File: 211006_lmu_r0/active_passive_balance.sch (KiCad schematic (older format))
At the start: 30 parts

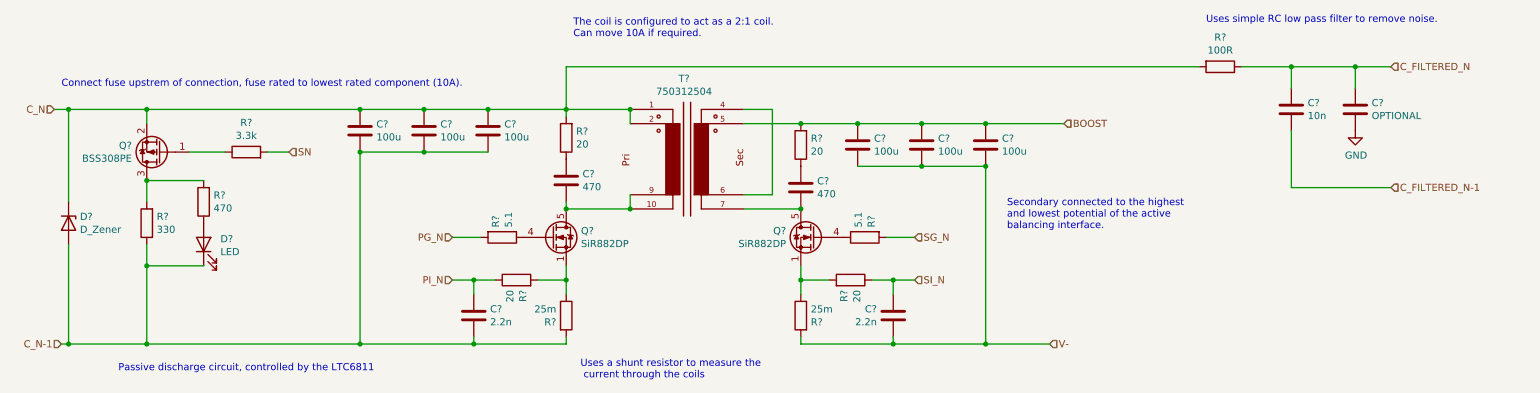
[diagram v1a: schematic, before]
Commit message: Updated BOM and footprints for non-hv components
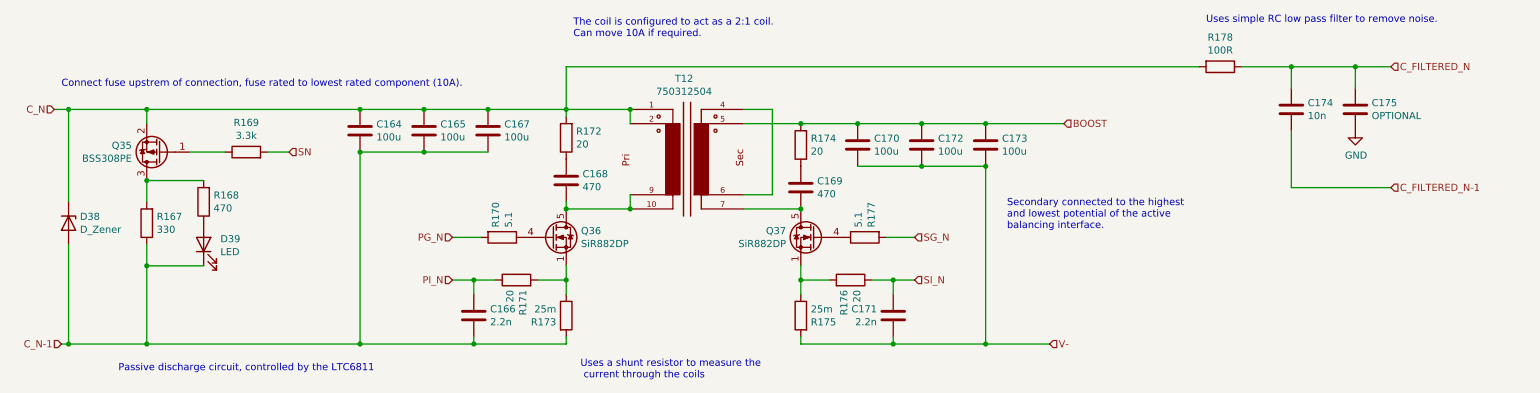
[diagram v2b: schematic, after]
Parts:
- gave numbers to parts that had none: 30

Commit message: Added most footprint requirements in HV
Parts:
- removed D19: D_Zener, symbol Device:D_Zener
- added D15: SBR10U200P5-13, DIO_SBR10U200P5-13, symbol SBR10U200P5-13:SBR10U200P5-13
- added TP21, TP22, TP23, TP24, TP25, TP26, TP27, TP28, TP29, TP30, TP31: TestPoint, symbol Connector:TestPoint
- C43, C49: footprint (none) -> Capacitor_SMD:C_1206_3216Metric_Pad1.33x1.80mm_HandSolder; Voltage (none) -> 100V
- C44, C46, C51, C52: footprint (none) -> Capacitor_SMD:C_1206_3216Metric_Pad1.33x1.80mm_HandSolder
- C45, C53: footprint (none) -> Capacitor_SMD:C_0603_1608Metric_Pad1.08x0.95mm_HandSolder
- C47, C48: footprint (none) -> Capacitor_SMD:C_0603_1608Metric_Pad1.08x0.95mm_HandSolder; Voltage (none) -> 100V
- C50: value 2.2n -> 470p; footprint (none) -> Capacitor_SMD:C_0603_1608Metric_Pad1.08x0.95mm_HandSolder
- C54: value OPTIONAL -> DNP 10n; footprint (none) -> Capacitor_SMD:C_0805_2012Metric_Pad1.18x1.45mm_HandSolder; Voltage (none) -> 100V
- D18: footprint (none) -> LED_SMD:LED_0805_2012Metric_Pad1.15x1.40mm_HandSolder
- R43, R48, R49, R50, R51: footprint (none) -> Resistor_SMD:R_1206_3216Metric_Pad1.30x1.75mm_HandSolder
- R44, R45, R46, R47, R52, R53, R54: footprint (none) -> Resistor_SMD:R_0603_1608Metric_Pad0.98x0.95mm_HandSolder
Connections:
- net C_FILTERED_N: now also TP31.1
- net C_N: now also D15.1, TP21.1; no longer C43.2
- net C_N-1: now also D15.2, D15.3
- net PG_N: now also TP23.1
- net PI_N: now also R47.2, TP24.1; no longer R47.1
- net SG_N: now also R53.1, TP29.1; no longer R53.2
- net SI_N: now also TP30.1
- net at Q5.3 (D), R43.2, R44.2: now also TP22.1
- net at Q7.4 (G): now also R53.2; no longer R53.1
- net at C47.1, Q6.5 (D), T2.10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: now also TP26.1
- net at C48.1, Q7.5 (D), T2.7: now also TP27.1
- net at Q6.1 (S), Q6.2 (S), Q6.3 (S)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: now also R47.1, TP25.1; no longer R47.2
- net at Q7.1 (S), Q7.2 (S), Q7.3 (S)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: now also TP28.1
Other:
- moved on the sheet: D39, Q35, R167, R168, R169

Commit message: Cleaned up last components missing footprint refs
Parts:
- TP21, TP22, TP23, TP24, TP25, TP26, TP27, TP28, TP29, TP30, TP31: footprint (none) -> TestPoint:TestPoint_Pad_D1.0mm

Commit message: Updated with Mouser links for BOM
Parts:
- C43, C44, C46, C49, C51, C52: value 100u -> 100uF
- C45: value 2.2n -> 2.2nF
- C47, C48: value 470 -> 470pF
- C50: value 470p -> 470pF
- C53: value 10n -> 10nF
- C54: value DNP 10n -> DNP 10nF
- D15: MANUFACTURER Diodes Inc -> (none); Manufacturer (none) -> Diodes Inc; Mouser Part Number (none) -> NOT AVAILABLE!; Mouser URL (none) -> NOT AVAILABLE!; Part Number (none) -> SBR10U200P5-13
- D18: value LED -> LED (Red); Manufacturer (none) -> AMS OSRAM; Mouser Part Number (none) -> 720-LSR976-NR-1; Mouser URL (none) -> https://au.mouser.com/ProductDetail/ams-OSRAM/LS-R976-NR-1-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; Part Number (none) -> LS R976-NR-1-0-20-R18
- Q5: Manufacturer (none) -> Infineon Technologies; Mouser Part Number (none) -> 726-BSS308PEH6327SA1; Mouser URL (none) -> https://au.mouser.com/ProductDetail/Infineon-Technologies/B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; Part Number (none) -> BSS308PEH6327XT
- Q6, Q7: Manufacturer (none) -> Vishay; Mouser Part Number (none) -> 78-SIR882DP-T1-GE3; Mouser URL (none) -> https://au.mouser.com/ProductDetail/Vishay-Semiconductors/S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; Part Number (none) -> SIR882DP-T1-GE3
- R43: value 330 -> 330R
- R44: value 470 -> 470R
- R45: value 3.3k -> 3.3kR
- R46, R53: value 5.1 -> 5.1R
- R47, R48, R50, R52: value 20 -> 20R
- R49, R51: value 25m -> 25mR
- T2: Manufacturer (none) -> Wurth; Mouser Part Number (none) -> NOT AVAILABLE!; Mouser URL (none) -> NOT AVAILABLE!; Part Number (none) -> 750312504
- TP26: renamed from TP21; Manufacturer (none) -> -; Mouser Part Number (none) -> -; Mouser URL (none) -> -; Part Number (none) -> -
- TP27: renamed from TP22; Manufacturer (none) -> -; Mouser Part Number (none) -> -; Mouser URL (none) -> -; Part Number (none) -> -
- TP28: renamed from TP23; Manufacturer (none) -> -; Mouser Part Number (none) -> -; Mouser URL (none) -> -; Part Number (none) -> -
- TP29: renamed from TP24; Manufacturer (none) -> -; Mouser Part Number (none) -> -; Mouser URL (none) -> -; Part Number (none) -> -
- TP30: renamed from TP25; Manufacturer (none) -> -; Mouser Part Number (none) -> -; Mouser URL (none) -> -; Part Number (none) -> -
- TP31: renamed from TP26; Manufacturer (none) -> -; Mouser Part Number (none) -> -; Mouser URL (none) -> -; Part Number (none) -> -
- TP32: renamed from TP27; Manufacturer (none) -> -; Mouser Part Number (none) -> -; Mouser URL (none) -> -; Part Number (none) -> -
- TP33: renamed from TP28; Manufacturer (none) -> -; Mouser Part Number (none) -> -; Mouser URL (none) -> -; Part Number (none) -> -
- TP34: renamed from TP29; Manufacturer (none) -> -; Mouser Part Number (none) -> -; Mouser URL (none) -> -; Part Number (none) -> -
- TP35: renamed from TP30; Manufacturer (none) -> -; Mouser Part Number (none) -> -; Mouser URL (none) -> -; Part Number (none) -> -
- TP36: renamed from TP31; Manufacturer (none) -> -; Mouser Part Number (none) -> -; Mouser URL (none) -> -; Part Number (none) -> -
